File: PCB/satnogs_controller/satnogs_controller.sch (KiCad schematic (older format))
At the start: 57 parts, among them P1 DEV-PINS, P2 End-Stops, P3 RJ45, P4 I2C, P7 Motor1, P8 Motor2, U1 ARDUINO_PRO_MINI, U2 MAX485, U3 POLOLU_A4988, U4 POLOLU_A4988, U5 TPS54360DDA, U6 POLOLU_DUAL_MC33926, U7 PCA9540B

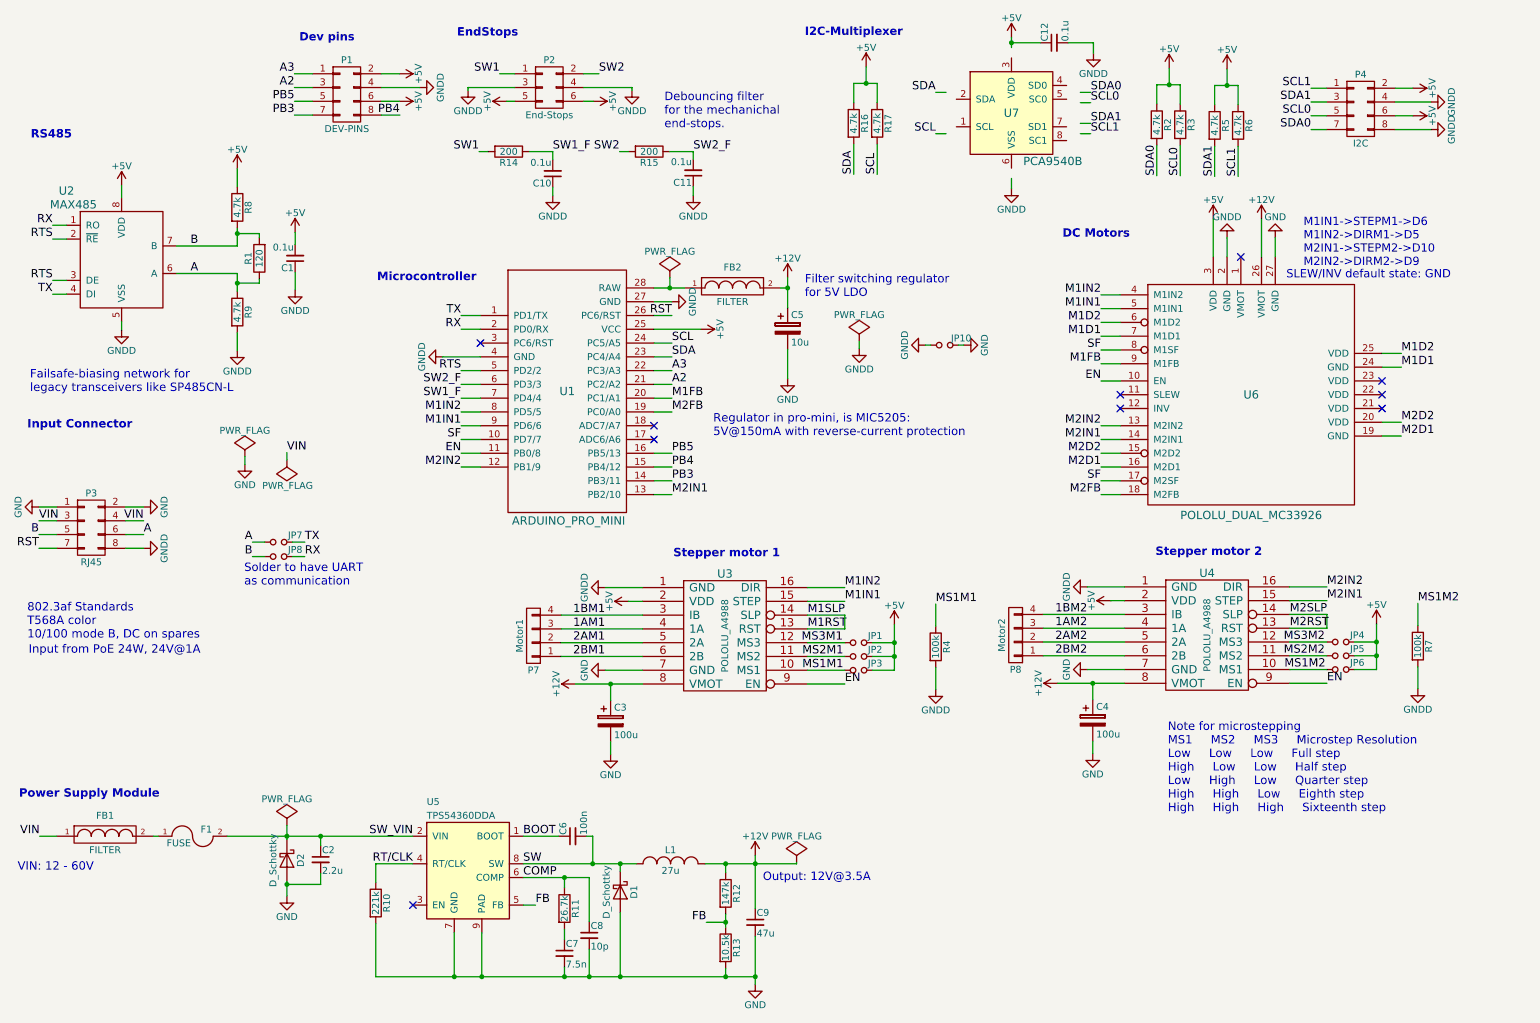
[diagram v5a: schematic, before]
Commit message: Resolve issues #22, #23, #24, #25
Signed-off-by: zisi <agzisim@gmail.com>
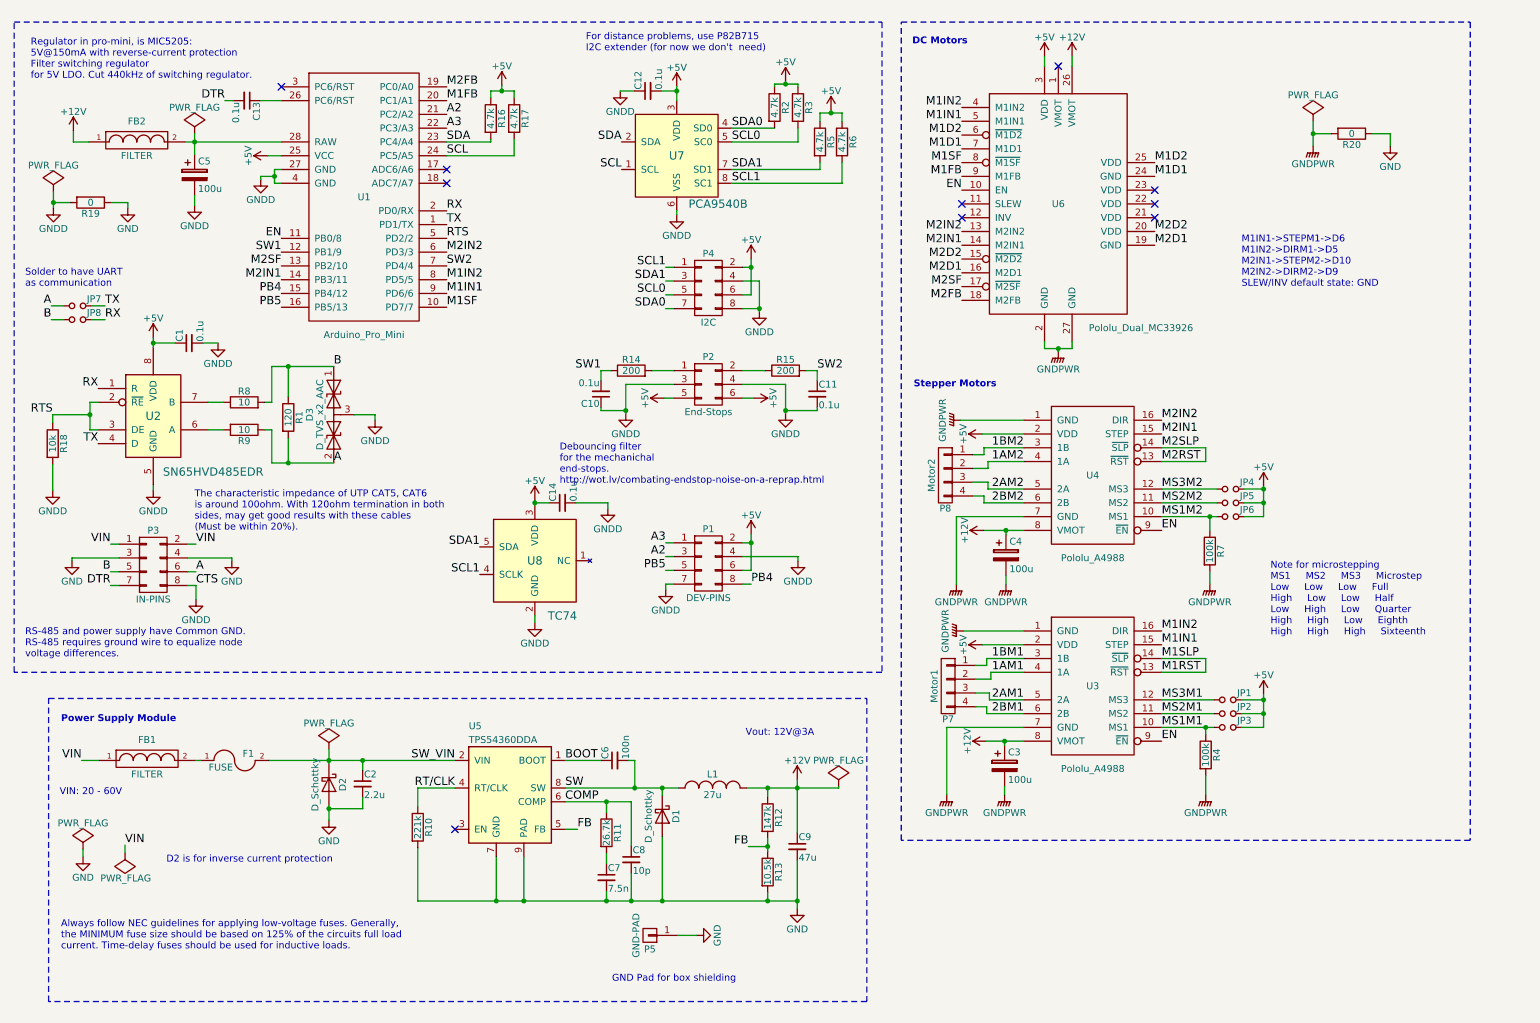
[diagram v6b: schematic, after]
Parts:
- removed JP10: Jumper_NO_Small, Resistors_SMD:R_0805_HandSoldering, symbol Jumper_NO_Small
- removed U1: ARDUINO_PRO_MINI, satnogs:arduino-pro-mini, symbol ARDUINO_PRO_MINI
- removed U2: MAX485, Housings_SOIC:SOIC-8_3.9x4.9mm_Pitch1.27mm, symbol MAX485
- removed U3, U4: POLOLU_A4988, satnogs:pololu-a4988, symbol POLOLU_A4988
- removed U6: POLOLU_DUAL_MC33926, satnogs:pololu-dual-mc33926, symbol POLOLU_DUAL_MC33926
- added C13, C14: 0.1u, Capacitors_SMD:C_0805_HandSoldering, symbol C_Small
- added D3: D_TVS_x2_AAC, TO_SOT_Packages_SMD:SOT-23_Handsoldering, symbol D_TVS_x2_AAC
- added P5: GND-PAD, Mounting_Holes:MountingHole_2.2mm_M2_DIN965_Pad, symbol CONN_01X01
- added R18: 10k, Resistors_SMD:R_0805_HandSoldering, symbol R
- added R19: 0, Resistors_SMD:R_0805_HandSoldering, symbol R
- added R20: 0, Resistors_SMD:R_1210_HandSoldering, symbol R
- added U1: Arduino_Pro_Mini, satnogs:Arduino_Pro_Mini, symbol Arduino_Pro_Mini
- added U2: SN65HVD485EDR, satnogs:SOIC-8_3.9x4.9mm_Pitch1.27mm_HandSoldering, symbol SN65HVD485EDR
- added U3, U4: Pololu_A4988, satnogs:Pololu_A4988, symbol Pololu_A4988
- added U6: Pololu_Dual_MC33926, satnogs:Pololu_Dual_MC33926, symbol Pololu_Dual_MC33926
- added U8: TC74, satnogs:SOT-23-5_HandSoldering, symbol TC74
- C1, C10, C11, C12: Mnf. VJ0805Y104KXJCW1BC -> 08053C104KAT2A; Price 0.118 -> 0.094
- C2, C9: footprint Capacitors_SMD:C_1210 -> Capacitors_SMD:C_1210_HandSoldering
- C5: value 10u -> 100u
- C6: Price 0.091 -> 0.094
- D1, D2: footprint Diodes_SMD:DO-214AB -> satnogs:DO-214AB_Handsoldering; Mnf. B560C-13-F -> CDBC560-G; Price 0.494 -> 0.67
- F1: footprint satnogs:mini-fuse-holder-3568 -> satnogs:FuseHolder_Keystone-3557-10; Mnf. Keystone Electronics, 3568 -> Keystone Electronics 3557-10; Price 0.732 -> 1.09
- FB1: Mnf. MPZ2012S300A -> BLM21PG221SN1D; Price 0.109 -> 0.104
- FB2: Mnf. MPZ2012S300A -> BLM21AG221SN1D; Price 0.109 -> 0.141
- JP1, JP2, JP3, JP4, JP5, JP6, JP7, JP8: Mnf. (none) -> CRCW08050000Z0EA; Price (none) -> 0.094
- L1: footprint satnogs:bourns-srr1210 -> satnogs:Inductor_Bourns-SRR1210_HandSoldering
- P1, P2, P4: Distributor SparkFun PRT-12791 -> (none); Manufacturer - -> (none); Notes https://www.sparkfun.com/products/12791 -> (none); Package 2x23 pin male PTH header -> (none); Price - -> (none)
- P3: value RJ45 -> IN-PINS; Distributor SparkFun PRT-12791 -> (none); Manufacturer - -> (none); Notes https://www.sparkfun.com/products/12791 -> (none); Package 2x23 pin male PTH header -> (none); Price - -> (none)
- P7, P8: footprint Connect:bornier4 -> satnogs:MKDS_1.5-4; Mnf. Altech - 30.704 -> Phoenix 1985467; Price 1.99 -> 0.7
- R14, R15: Mnf. CRCW08054K70JNEA -> CRCW0805200RJNEA
- R4: Notes 1/8W 5% -> (none)
- R8: value 4.7k -> 10; Mnf. CRCW08054K70JNEA -> CRCW080510R0JNEA
- R9: value 4.7k -> 10; Manufacturer CRCW08054K70JNEA -> (none); Mnf. (none) -> CRCW080510R0JNEA
- U5: Price 4.53 -> 4
- U7: footprint Housings_SSOP:TSSOP-8_3x3mm_Pitch0.65mm -> satnogs:TSSOP-8_3x3mm_Pitch0.65mm_HandSoldering; Mnf. PCA9540BDP,118 -> PCA9540BDP 118; Price 1.18 -> 1.23
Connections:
- net labels added: CTS, DTR, GNDPWR, M1SF, M2SF
- net labels removed: PB3, RST, SF, SW1_F, SW2_F
- wire segments 231 -> 233
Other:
- note added: "Always follow NEC guidelines for applying low-voltage fuses. Generally,\nthe MINIMUM fuse size should be based on 125% of the circuits full load\ncurrent. Time-delay fuses should be used for inductive loads."
- note added: "D2 is for inverse current protection"
- note added: "Debouncing filter\nfor the mechanichal\nend-stops.\nhttp://wot.lv/combating-endstop-noise-on-a-reprap.html\n"
- note added: "GND Pad for box shielding"
- note added: "M1IN1->STEPM1->D6\nM1IN2->DIRM1->D5\nM2IN1->STEPM2->D10\nM2IN2->DIRM2->D9\nSLEW/INV default state: GND"
- note added: "Note for microstepping\nMS1 MS2 MS3 Microstep\nLow Low Low Full\nHigh Low Low Half\nLow High Low Quarter\nHigh High Low Eighth\nHigh High High Sixteenth"
- note added: "RS-485 and power supply have Common GND.\nRS-485 requires ground wire to equalize node\nvoltage differences."
- note added: "Regulator in pro-mini, is MIC5205:\n5V@150mA with reverse-current protection\nFilter switching regulator\nfor 5V LDO. Cut 440kHz of switching regulator."
- note added: "Stepper Motors"
- note added: "The characteristic impedance of UTP CAT5, CAT6\nis around 100ohm. With 120ohm termination in both\nsides, may get good results with these cables\n(Must be within 20%)."
- note added: "VIN: 20 - 60V"
- note added: "Vout: 12V@3A"
- note added: "\nFor distance problems, use P82B715\nI2C extender (for now we don't need)"
- note removed: "802.3af Standards\nT568A color\n10/100 mode B, DC on spares"
- note removed: "Debouncing filter\nfor the mechanichal\nend-stops.\n"
- note removed: "Dev pins"
- note removed: "EndStops"
- note removed: "Failsafe-biasing network for \nlegacy transceivers like SP485CN-L\n"
- note removed: "Filter switching regulator\nfor 5V LDO"
- note removed: "I2C-Multiplexer"
- note removed: "Input Connector"
- note removed: "Input from PoE 24W, 24V@1A"
- note removed: "M1IN1->STEPM1->D6\nM1IN2->DIRM1->D5\nM2IN1->STEPM2->D10\nM2IN2->DIRM2->D9"
- note removed: "Microcontroller"
- note removed: "Note for microstepping\nMS1 MS2 MS3 Microstep Resolution\nLow Low Low Full step\nHigh Low Low Half step\nLow High Low Quarter step\nHigh High Low Eighth step\nHigh High High Sixteenth step"
- note removed: "Output: 12V@3.5A"
- note removed: "RS485"
- note removed: "Regulator in pro-mini, is MIC5205:\n5V@150mA with reverse-current protection"
- note removed: "SLEW/INV default state: GND"
- note removed: "Stepper motor 1"
- note removed: "Stepper motor 2"
- note removed: "VIN: 12 - 60V"
- moved on the sheet: C1, C10, C11, C12, C2, C3, C4, C5, C6, C7, C8, C9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

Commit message: Use one GND bottom plane and GND areas in front
Remove zero ohm resistors
To avoid connection with GNDD directly with motor GND use keep out area

Signed-off-by: zisi <agzisim@gmail.com>
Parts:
- removed R19: 0, Resistors_SMD:R_0805_HandSoldering, symbol R
- removed R20: 0, Resistors_SMD:R_1210_HandSoldering, symbol R
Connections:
- net GNDD is gone; now on net GND: C1.2, C10.1, C11.2, C12.1, C14.2, C5.2, D3.3 (common), P1.4 (P4), P1.7 (P7), P2.3 (P3), P2.4 (P4), P3.8 (P8), P4.4 (P4), P4.8 (P8), R18.2, U1.27 (GND), U1.4 (GND), U2.5 (GND), U7.6 (VSS), U8.2 (GND)
- net GNDPWR is gone; now on net GND: C3.2, C4.2, R4.2, R7.2, U3.1 (GND), U3.7 (GND), U4.1 (GND), U4.7 (GND), U6.2 (GND), U6.27 (GND)

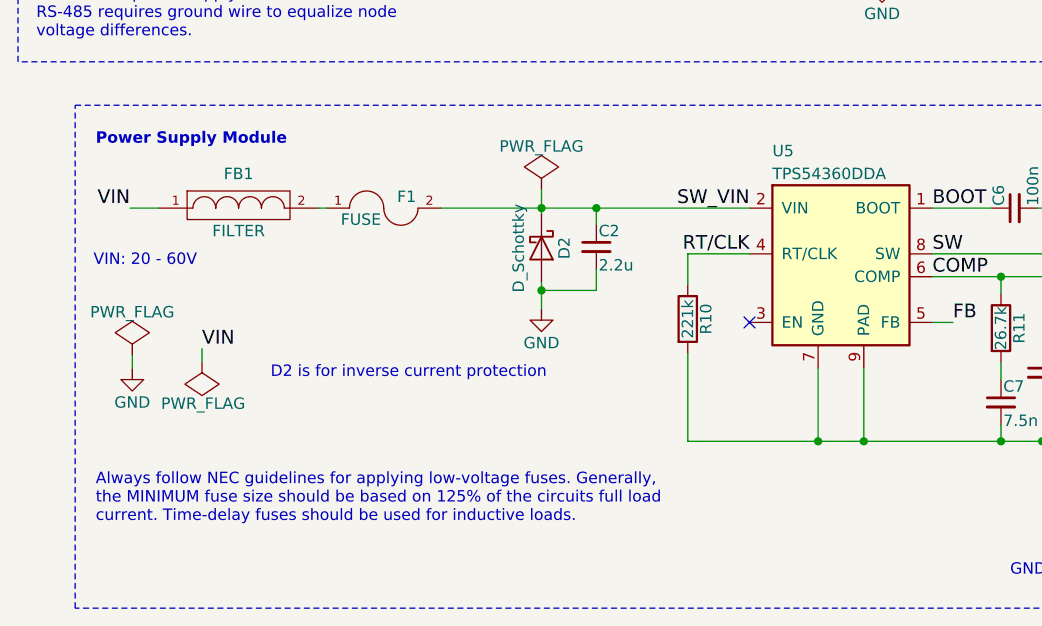
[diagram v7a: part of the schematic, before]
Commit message: Add electrolytic capacitor, TVS-diode in PSU input
Capacitor reduces the voltage ripple of input voltage (long cable)
TVS-diode protect the PSU and all the board from surges and ESD events

Signed-off-by: zisi <agzisim@gmail.com>
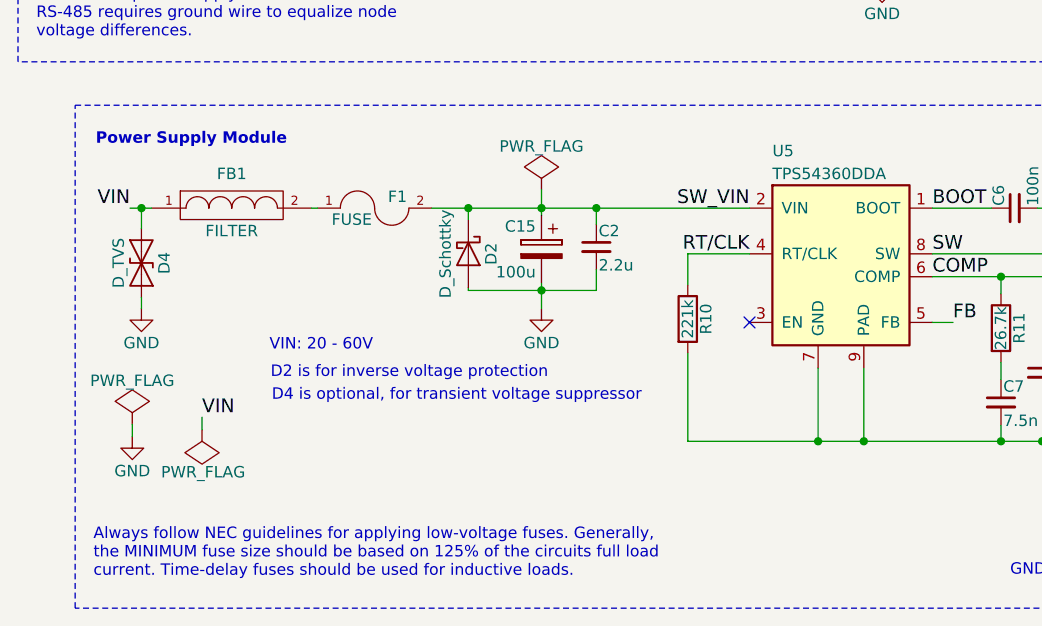
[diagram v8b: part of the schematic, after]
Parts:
- added C15: 100u, satnogs:CP_Radial_D10.0mm_P5.00mm, symbol CP
- added D4: D_TVS, satnogs:DO-214AB_Handsoldering, symbol D_TVS
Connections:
- net GND: now also C15.2, D4.2 (A2)
- net SW_VIN: now also C15.1
- net VIN: now also D4.1 (A1)
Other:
- note added: "D2 is for inverse voltage protection"
- note added: "D4 is optional, for transient voltage suppressor"
- note removed: "D2 is for inverse current protection"
- moved on the sheet: D2, F1, FB1
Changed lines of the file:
@@
 L PWR_FLAG #FLG04
 U 1 1 568E938B
-P 1345 6590
-F 0 "#FLG04" H 1345 6685 50  0001 C CNN
-F 1 "PWR_FLAG" H 1340 6775 50  0000 C CNN
-F 2 "" H 1345 6590 60  0000 C CNN
-F 3 "" H 1345 6590 60  0000 C CNN
-	1    1345 6590
+P 1345 6890
+F 0 "#FLG04" H 1345 6985 50  0001 C CNN
+F 1 "PWR_FLAG" H 1340 7075 50  0000 C CNN
+F 2 "" H 1345 6890 60  0000 C CNN
+F 3 "" H 1345 6890 60  0000 C CNN
+	1    1345 6890
 	-1   0    0    1
 $EndComp
@@
 L FILTER FB1
 U 1 1 57E7000D
-P 1505 5920
-F 0 "FB1" H 1505 6070 50  0000 C CNN
-F 1 "FILTER" H 1505 5820 50  0000 C CNN
-F 2 "Resistors_SMD:R_0805_HandSoldering" H 1505 5920 50  0001 C CNN
-F 3 "" H 1505 5920 50  0001 C CNN
-F 4 "BLM21PG221SN1D" H 1505 5920 60  0001 C CNN "Mnf."
-F 5 "0.104" H 1505 5920 60  0001 C CNN "Price"
-	1    1505 5920
+P 1475 5920
+F 0 "FB1" H 1475 6070 50  0000 C CNN
+F 1 "FILTER" H 1475 5820 50  0000 C CNN
+F 2 "Resistors_SMD:R_0805_HandSoldering" H 1475 5920 50  0001 C CNN
+F 3 "" H 1475 5920 50  0001 C CNN
+F 4 "BLM21PG221SN1D" H 1475 5920 60  0001 C CNN "Mnf."
+F 5 "0.104" H 1475 5920 60  0001 C CNN "Price"
+	1    1475 5920
 	1    0    0    -1
 $EndComp
@@
 L FUSE F1
 U 1 1 57E70188
-P 2140 5920
-F 0 "F1" H 2240 5970 50  0000 C CNN
-F 1 "FUSE" H 2040 5870 50  0000 C CNN
-F 2 "satnogs:FuseHolder_Keystone-3557-10" H 2140 5920 50  0001 C CNN
-F 3 "" H 2140 5920 50  0001 C CNN
-F 4 "Keystone Electronics 3557-10" H 2140 5920 60  0001 C CNN "Mnf."
-F 5 "1.09" H 2140 5920 60  0001 C CNN "Price"
-	1    2140 5920
+P 2100 5920
+F 0 "F1" H 2200 5970 50  0000 C CNN
+F 1 "FUSE" H 2000 5870 50  0000 C CNN
+F 2 "satnogs:FuseHolder_Keystone-3557-10" H 2100 5920 50  0001 C CNN
+F 3 "" H 2100 5920 50  0001 C CNN
+F 4 "Keystone Electronics 3557-10" H 2100 5920 60  0001 C CNN "Mnf."
+F 5 "1.09" H 2100 5920 60  0001 C CNN "Price"
+	1    2100 5920
 	1    0    0    -1
 $EndComp
@@
 Text Label 1240 4350 2    60   ~ 0
 VIN
-Text Label 1345 6535 0    60   ~ 0
+Text Label 1345 6835 0    60   ~ 0
 VIN
 $Comp
@@
 L D_Schottky D2
 U 1 1 57E9650D
-P 2830 6095
-F 0 "D2" H 2830 6195 50  0000 C CNN
-F 1 "D_Schottky" H 2830 5995 50  0000 C CNN
-F 2 "satnogs:DO-214AB_Handsoldering" H 2830 6095 50  0001 C CNN
-F 3 "" H 2830 6095 50  0000 C CNN
-F 4 "CDBC560-G" H 2830 6095 60  0001 C CNN "Mnf."
-F 5 "0.67" H 2830 6095 60  0001 C CNN "Price"
-	1    2830 6095
+P 2510 6120
+F 0 "D2" H 2510 6220 50  0000 C CNN
+F 1 "D_Schottky" H 2510 6020 50  0000 C CNN
+F 2 "satnogs:DO-214AB_Handsoldering" H 2510 6120 50  0001 C CNN
+F 3 "" H 2510 6120 50  0000 C CNN
+F 4 "CDBC560-G" H 2510 6120 60  0001 C CNN "Mnf."
+F 5 "0.67" H 2510 6120 60  0001 C CNN "Price"
+	1    2510 6120
 	0    1    1    0
 $EndComp
@@
 	0    -1   -1   0
 $EndComp
-Text Notes 870  6180 0    50   ~ 0
+Text Notes 1640 6550 0    50   ~ 0
 VIN: 20 - 60V
 $Comp
@@
 L PWR_FLAG #FLG017
 U 1 1 582A772F
-P 1040 6565
-F 0 "#FLG017" H 1040 6660 50  0001 C CNN
-F 1 "PWR_FLAG" H 1040 6755 50  0000 C CNN
-F 2 "" H 1040 6565 60  0000 C CNN
-F 3 "" H 1040 6565 60  0000 C CNN
-	1    1040 6565
+P 1040 6865
+F 0 "#FLG017" H 1040 6960 50  0001 C CNN
+F 1 "PWR_FLAG" H 1040 7055 50  0000 C CNN
+F 2 "" H 1040 6865 60  0000 C CNN
+F 3 "" H 1040 6865 60  0000 C CNN
+	1    1040 6865
 	1    0    0    -1
 $EndComp
@@
 L GND #PWR018
 U 1 1 582A7F4E
-P 1040 6620
-F 0 "#PWR018" H 1040 6370 50  0001 C CNN
-F 1 "GND" H 1040 6470 50  0000 C CNN
-F 2 "" H 1040 6620 60  0000 C CNN
-F 3 "" H 1040 6620 60  0000 C CNN
-	1    1040 6620
+P 1040 6920
+F 0 "#PWR018" H 1040 6670 50  0001 C CNN
+F 1 "GND" H 1040 6770 50  0000 C CNN
+F 2 "" H 1040 6920 60  0000 C CNN
+F 3 "" H 1040 6920 60  0000 C CNN
+	1    1040 6920
 	1    0    0    -1
 $EndComp
@@
 \nFor distance problems, use P82B715\nI2C extender (for now we don't  need)
 Text Notes 1645 6670 0    50   ~ 0
-D2 is for inverse current protection
-Text Notes 880  7300 0    50   ~ 0
+D2 is for inverse voltage protection
+Text Notes 870  7540 0    50   ~ 0
 Always follow NEC guidelines for applying low-voltage fuses. Generally,\nthe MINIMUM fuse size should be based on 125% of the circuits full load\ncurrent. Time-delay fuses should be used for inductive loads.
 $Comp
@@
 $EndComp
 Wire Wire Line
-	1345 6590 1345 6535
-Wire Wire Line
-	2830 6245 2830 6360
-Wire Wire Line
-	1155 5920 1030 5920
-Wire Wire Line
-	2830 5840 2830 5945
-Wire Wire Line
-	2390 5920 3740 5920
+	1345 6890 1345 6835
+Wire Wire Line
+	1125 5920 1030 5920
+Wire Wire Line
+	2350 5920 3740 5920
 Connection ~ 2830 5920
 Wire Wire Line
-	1855 5920 1890 5920
+	1825 5920 1850 5920
 Wire Wire Line
 	3070 5920 3070 5990
@@
 Connection ~ 5045 6120
 Wire Wire Line
-	1040 6620 1040 6565
+	1040 6920 1040 6865
 Wire Wire Line
 	5355 7190 5495 7190
@@
 	5270 4640 5270 4680
 Connection ~ 2830 6280
-Wire Wire Line
-	3070 6280 2830 6280
+$Comp
+L CP C15
+U 1 1 589F63F7
+P 2830 6100
+F 0 "C15" H 2855 6200 50  0000 L CNN
+F 1 "100u" H 2855 6000 50  0000 L CNN
+F 2 "satnogs:CP_Radial_D10.0mm_P5.00mm" H 2868 5950 30  0001 C CNN
+F 3 "" H 2830 6100 60  0001 C CNN
+F 4 "RGA101M1JBK-1012G" H 2830 6100 60  0001 C CNN "Mnf."
+F 5 "0.248" H 2830 6100 60  0001 C CNN "Price"
+	1    2830 6100
+	-1   0    0    -1
+$EndComp
+$Comp
+L GND #PWR058
+U 1 1 589F7873
+P 1080 6360
+F 0 "#PWR058" H 1080 6110 50  0001 C CNN
+F 1 "GND" H 1080 6210 50  0000 C CNN
+F 2 "" H 1080 6360 60  0000 C CNN
+F 3 "" H 1080 6360 60  0000 C CNN
+	1    1080 6360
+	1    0    0    -1
+$EndComp
+Wire Wire Line
+	2510 6280 3070 6280
+Wire Wire Line
+	2830 6250 2830 6360
+Wire Wire Line
+	2830 5840 2830 5950
+Wire Wire Line
+	2510 5970 2510 5920
+Connection ~ 2510 5920
+Wire Wire Line
+	2510 6270 2510 6280
+$Comp
+L D_TVS D4
+U 1 1 58A4445A
+P 1080 6160
+F 0 "D4" H 1080 6260 50  0000 C CNN
+F 1 "D_TVS" H 1080 6060 50  0000 C CNN
+F 2 "satnogs:DO-214AB_Handsoldering" H 1080 6160 50  0001 C CNN
+F 3 "" H 1080 6160 50  0000 C CNN
+F 4 "SMCJ48A-E3/57T" H 1080 6160 60  0001 C CNN "Mnf."
+F 5 "0.472" H 1080 6160 60  0001 C CNN "Price"
+	1    1080 6160
+	0    1    1    0
+$EndComp
+Wire Wire Line
+	1080 6010 1080 5920
+Connection ~ 1080 5920
+Wire Wire Line
+	1080 6360 1080 6310
+Text Notes 1650 6770 0    50   ~ 0
+D4 is optional, for transient voltage suppressor
 $EndSCHEMATC
